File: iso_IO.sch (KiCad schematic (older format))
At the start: 32 parts, among them J9 AVR-ISP-6, Q7 Q_NMOS_GDS, U10 AM26LV32xD, U11 ADuM120N, U12 ADuM120N, U13 PC355, U9 ATtiny13A-SU

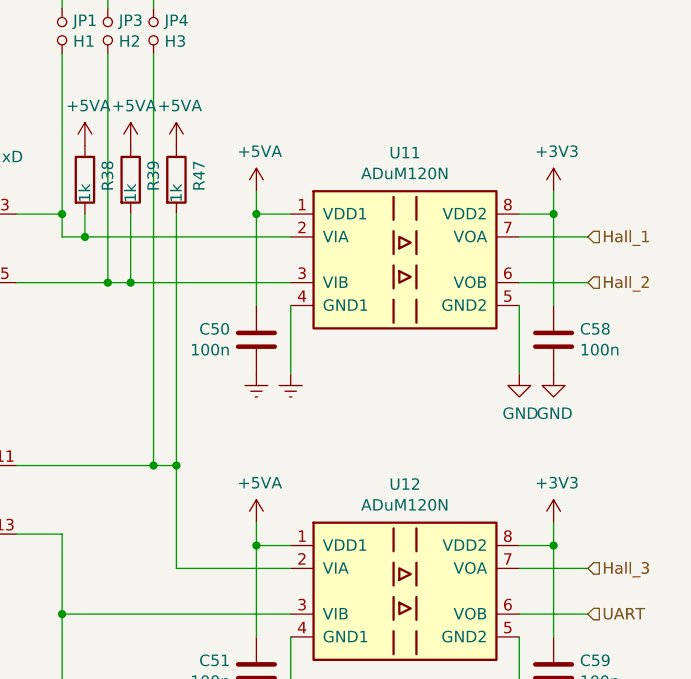
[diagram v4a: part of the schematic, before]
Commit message: - renamed ADUM3054 as ADM3054 - specified ADuM120N1 (fail high)
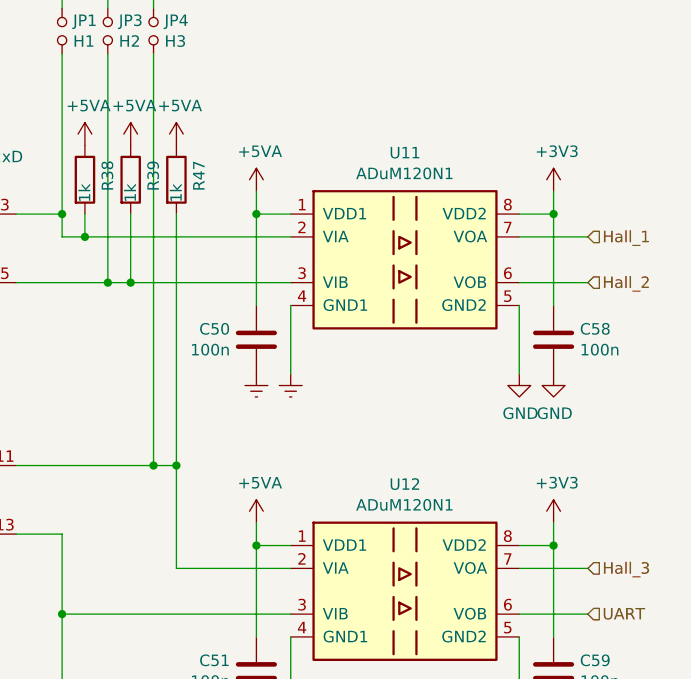
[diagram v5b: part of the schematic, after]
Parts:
- U11, U12: value ADuM120N -> ADuM120N1
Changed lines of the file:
@@
 P 5300 1850
 F 0 "U11" H 5300 2317 50  0000 C CNN
-F 1 "ADuM120N" H 5300 2226 50  0000 C CNN
+F 1 "ADuM120N1" H 5300 2226 50  0000 C CNN
 F 2 "Package_SO:SOIC-8_3.9x4.9mm_P1.27mm" H 5300 1450 50  0001 C CIN
 F 3 "https://www.analog.com/media/en/technical-documentation/data-sheets/ADuM120N_121N.pdf" H 4850 2250 50  0001 C CNN
@@
 P 5300 3300
 F 0 "U12" H 5300 3767 50  0000 C CNN
-F 1 "ADuM120N" H 5300 3676 50  0000 C CNN
+F 1 "ADuM120N1" H 5300 3676 50  0000 C CNN
 F 2 "Package_SO:SOIC-8_3.9x4.9mm_P1.27mm" H 5300 2900 50  0001 C CIN
 F 3 "https://www.analog.com/media/en/technical-documentation/data-sheets/ADuM120N_121N.pdf" H 4850 3700 50  0001 C CNN

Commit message: - updated schematic symbols - updated silk screen version label
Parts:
- JP1, JP3, JP4: symbol Device:Jumper_NO_Small -> Jumper:Jumper_2_Open
- U9: symbol MCU_Microchip_ATtiny:ATtiny13A-SU -> MCU_Microchip_ATtiny:ATtiny13-20S
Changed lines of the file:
@@
 $EndComp
 $Comp
-L Device:Jumper_NO_Small JP1
+L Jumper:Jumper_2_Open JP1
 U 1 1 5E6645D9
-P 3800 850
-F 0 "JP1" V 3754 898 50  0000 L CNN
-F 1 "H1" V 3845 898 50  0000 L CNN
-F 2 "Jumper:SolderJumper-2_P1.3mm_Open_TrianglePad1.0x1.5mm" H 3800 850 50  0001 C CNN
-F 3 "~" H 3800 850 50  0001 C CNN
-	1    3800 850
+P 3800 900
+F 0 "JP1" V 3754 948 50  0000 L CNN
+F 1 "H1" V 3845 948 50  0000 L CNN
+F 2 "Jumper:SolderJumper-2_P1.3mm_Open_TrianglePad1.0x1.5mm" H 3800 900 50  0001 C CNN
+F 3 "~" H 3800 900 50  0001 C CNN
+	1    3800 900
 	0    1    1    0
 $EndComp
 $Comp
-L Device:Jumper_NO_Small JP3
-U 1 1 5E6654E8
-P 4000 850
-F 0 "JP3" V 3954 898 50  0000 L CNN
-F 1 "H2" V 4045 898 50  0000 L CNN
-F 2 "Jumper:SolderJumper-2_P1.3mm_Open_TrianglePad1.0x1.5mm" H 4000 850 50  0001 C CNN
-F 3 "~" H 4000 850 50  0001 C CNN
-	1    4000 850
+L Jumper:Jumper_2_Open JP4
+U 1 1 5E665A0A
+P 4200 900
+F 0 "JP4" V 4154 948 50  0000 L CNN
+F 1 "H3" V 4245 948 50  0000 L CNN
+F 2 "Jumper:SolderJumper-2_P1.3mm_Open_TrianglePad1.0x1.5mm" H 4200 900 50  0001 C CNN
+F 3 "~" H 4200 900 50  0001 C CNN
+	1    4200 900
 	0    1    1    0
 $EndComp
-$Comp
-L Device:Jumper_NO_Small JP4
-U 1 1 5E665A0A
-P 4200 850
-F 0 "JP4" V 4154 898 50  0000 L CNN
-F 1 "H3" V 4245 898 50  0000 L CNN
-F 2 "Jumper:SolderJumper-2_P1.3mm_Open_TrianglePad1.0x1.5mm" H 4200 850 50  0001 C CNN
-F 3 "~" H 4200 850 50  0001 C CNN
-	1    4200 850
-	0    1    1    0
-$EndComp
-Wire Wire Line
-	3800 950  3800 1650
 Wire Wire Line
 	3800 1750 3900 1750
@@
 Wire Wire Line
 	3800 1650 3800 1750
-Wire Wire Line
-	4000 950  4000 1950
 Connection ~ 4000 1950
 Wire Wire Line
 	4000 1950 4100 1950
-Wire Wire Line
-	4200 950  4200 2750
 Connection ~ 4200 2750
 Wire Wire Line
 	3600 2750 4200 2750
-Wire Wire Line
-	3800 750  3800 700
 Wire Wire Line
 	3800 700  2200 700
@@
 	2200 1550 2000 1550
 Wire Wire Line
-	4000 750  4000 650
-Wire Wire Line
 	4000 650  2150 650
 Wire Wire Line
@@
 	2150 1850 2000 1850
 Wire Wire Line
-	4200 750  4200 600
-Wire Wire Line
 	4200 600  2100 600
 Wire Wire Line
@@
 	3600 3050 3800 3050
 $Comp
-L MCU_Microchip_ATtiny:ATtiny13A-SU U9
+L MCU_Microchip_ATtiny:ATtiny13-20S U9
 U 1 1 5E67C6EE
 P 3050 5850
@@
 Wire Wire Line
 	3800 3400 3800 5650
+$Comp
+L Jumper:Jumper_2_Open JP3
+U 1 1 5E6654E8
+P 4000 900
+F 0 "JP3" V 3954 948 50  0000 L CNN
+F 1 "H2" V 4045 948 50  0000 L CNN
+F 2 "Jumper:SolderJumper-2_P1.3mm_Open_TrianglePad1.0x1.5mm" H 4000 900 50  0001 C CNN
+F 3 "~" H 4000 900 50  0001 C CNN
+	1    4000 900
+	0    1    1    0
+$EndComp
+Wire Wire Line
+	3800 1100 3800 1650
+Wire Wire Line
+	4000 700  4000 650
+Wire Wire Line
+	4000 1100 4000 1950
+Wire Wire Line
+	4200 700  4200 600
+Wire Wire Line
+	4200 1100 4200 2750
 $EndSCHEMATC
